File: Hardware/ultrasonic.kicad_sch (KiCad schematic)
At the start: 74 parts, among them J4 DG250-3-5-02P-11-00AH, Q1 BC817-40, Q2 BC817-40, Q3 BCP53-16, Q4 BCP56-16, Q5 BCP53-16, Q6 BCP56-16, Q7 MJD45H11T4G, Q8 MJD44H11T4G, U4 AD8656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

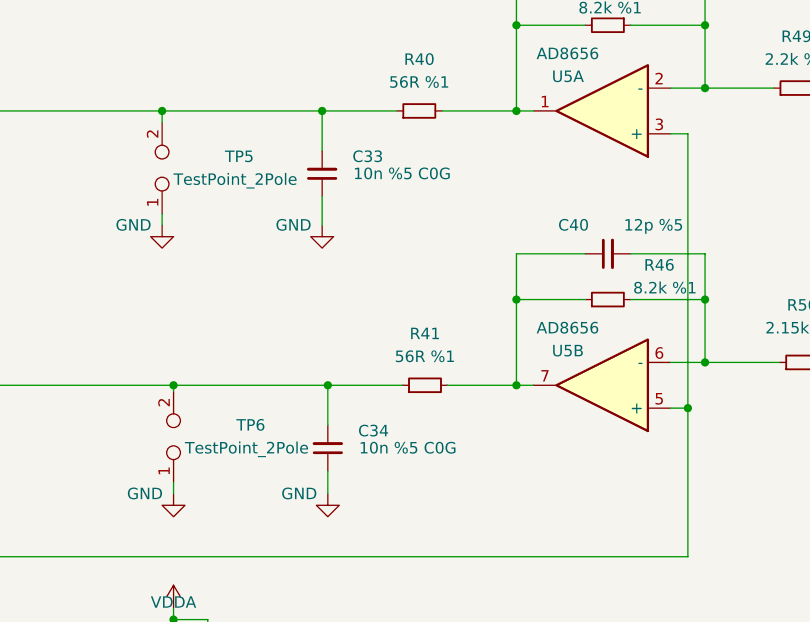
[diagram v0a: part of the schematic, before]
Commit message: Few coonector footprint modifications and silkscreen additions to them.
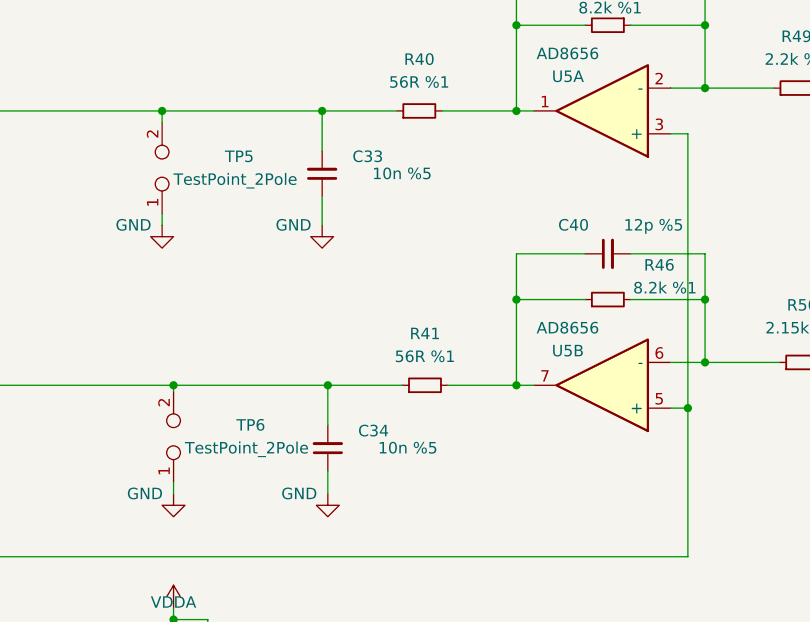
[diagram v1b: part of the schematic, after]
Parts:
- C33, C34: value 10n %5 C0G -> 10n %5; Link https://ozdisan.com/passive-components/capacitors/smt-smd-and-mlcc-capacitors/CL10C103JA8NNNC -> https://ozdisan.com/passive-components/capacitors/smt-smd-and-mlcc-capacitors/GRM1885C1H103JA01D; Price 0.07588 -> 0.04050
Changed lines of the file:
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@@
     (in_bom yes) (on_board yes)
     (property "Reference" "C34" (id 0) (at 179.705 151.13 0))
-    (property "Value" "10n %5 C0G" (id 1) (at 183.515 153.035 0))
+    (property "Value" "10n %5" (id 1) (at 183.515 153.035 0))
     (property "Footprint" "Capacitor_SMD:C_0603_1608Metric_Pad1.08x0.95mm_HandSolder" (id 2) (at 174.625 153.035 0)
       (effects (font (size 1.27 1.27)) hide)
@@
       (effects (font (size 1.27 1.27)) hide)
     )
-    (property "Link" "https://ozdisan.com/passive-components/capacitors/smt-smd-and-mlcc-capacitors/CL10C103JA8NNNC" (id 4) (at 174.625 153.035 0)
+    (property "Link" "https://ozdisan.com/passive-components/capacitors/smt-smd-and-mlcc-capacitors/GRM1885C1H103JA01D" (id 4) (at 174.625 153.035 0)
       (effects (font (size 1.27 1.27)) hide)
     )
-    (property "Price" "0.07588" (id 5) (at 174.625 153.035 0)
+    (property "Price" "0.04050" (id 5) (at 174.625 153.035 0)
       (effects (font (size 1.27 1.27)) hide)
     )
@@
     (in_bom yes) (on_board yes)
     (property "Reference" "C33" (id 0) (at 179.07 120.65 0))
-    (property "Value" "10n %5 C0G" (id 1) (at 182.88 122.555 0))
+    (property "Value" "10n %5" (id 1) (at 182.88 122.555 0))
     (property "Footprint" "Capacitor_SMD:C_0603_1608Metric_Pad1.08x0.95mm_HandSolder" (id 2) (at 173.99 122.555 0)
       (effects (font (size 1.27 1.27)) hide)
@@
       (effects (font (size 1.27 1.27)) hide)
     )
-    (property "Link" "https://ozdisan.com/passive-components/capacitors/smt-smd-and-mlcc-capacitors/CL10C103JA8NNNC" (id 4) (at 173.99 122.555 0)
+    (property "Link" "https://ozdisan.com/passive-components/capacitors/smt-smd-and-mlcc-capacitors/GRM1885C1H103JA01D" (id 4) (at 173.99 122.555 0)
       (effects (font (size 1.27 1.27)) hide)
     )
-    (property "Price" "0.07588" (id 5) (at 173.99 122.555 0)
+    (property "Price" "0.04050" (id 5) (at 173.99 122.555 0)
       (effects (font (size 1.27 1.27)) hide)
     )

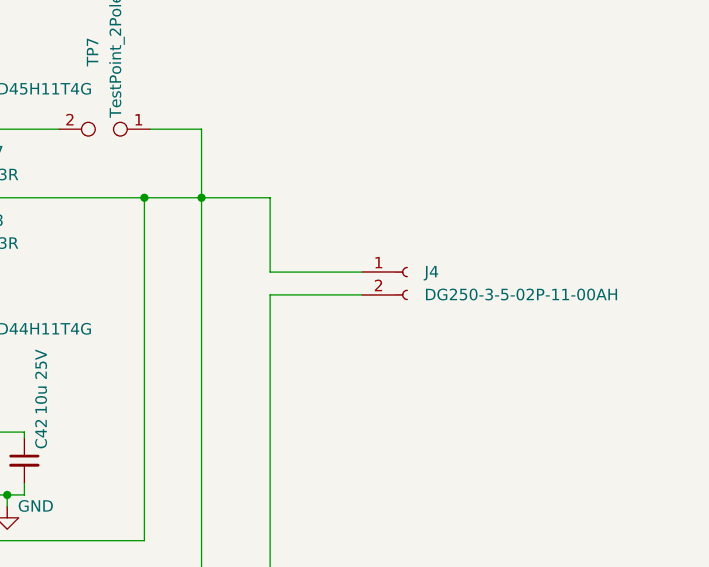
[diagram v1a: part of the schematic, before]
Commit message: Toolchain set. Timer module added. Schematic files migrated.
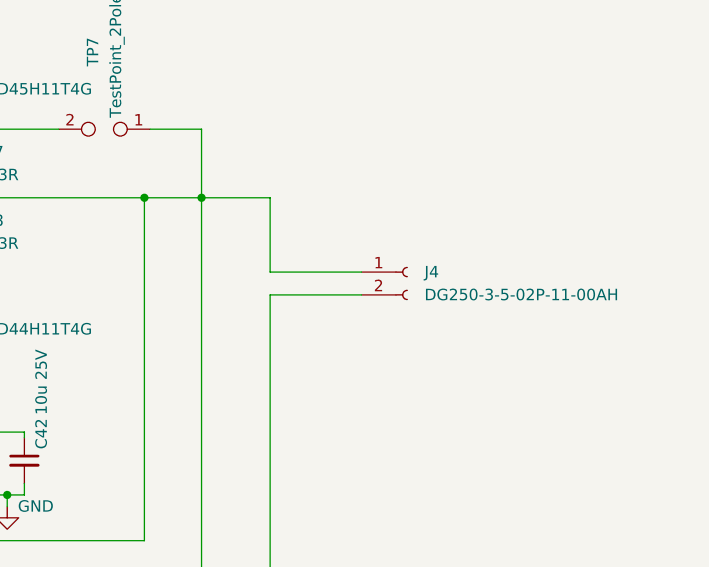
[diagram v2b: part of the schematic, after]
